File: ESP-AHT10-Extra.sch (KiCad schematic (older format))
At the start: 29 parts, among them J1 USB, SW1 RESET, SW2 PROG, U1 CH330N, U2 HT7233, U3 ESP-12, U4 AHT10, U5 USBLC6-2SC6

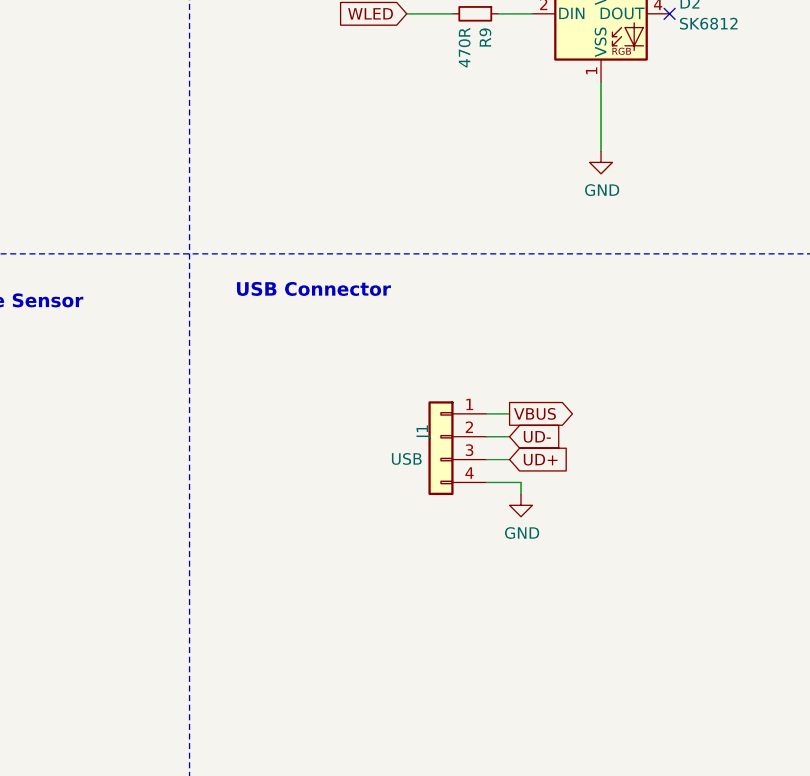
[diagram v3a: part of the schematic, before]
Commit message: place WLED, tidy up after some footprint changes
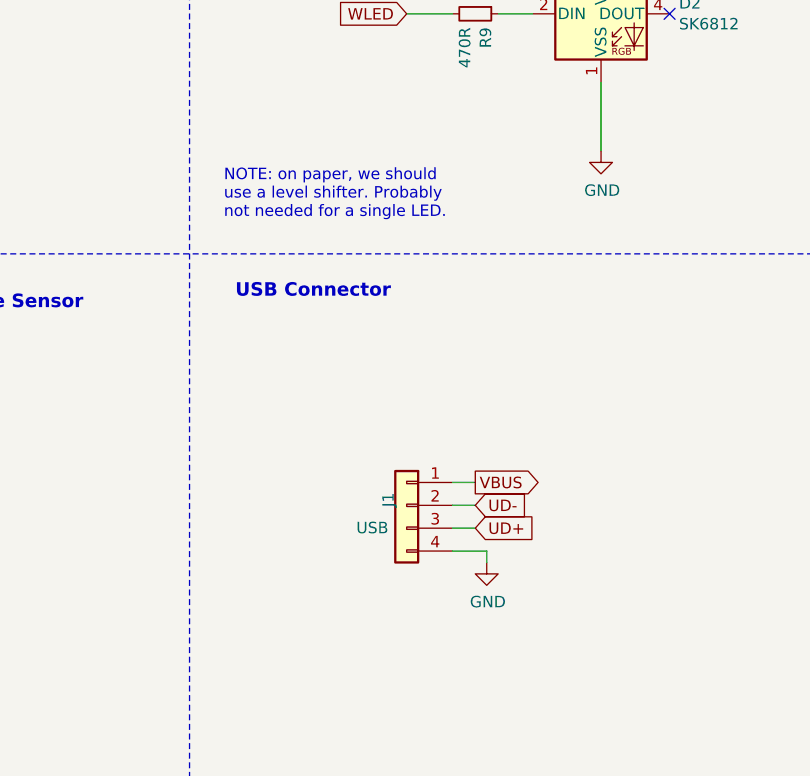
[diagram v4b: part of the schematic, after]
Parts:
- C1, C2, C3, C4, C5, C6, C7, C8: footprint Capacitors_SMD:C_0805 -> Capacitor_SMD:C_0805_2012Metric
- C9: footprint (none) -> Capacitor_SMD:C_0805_2012Metric
- D1: footprint Diodes_SMD:D_SOD-123F -> Diode_SMD:D_SOD-123F
- R1, R2, R3, R4, R5, R6, R7, R8, R9: footprint Resistors_SMD:R_0805 -> Resistor_SMD:R_0805_2012Metric
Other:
- note added: "NOTE: on paper, we should\nuse a level shifter. Probably\nnot needed for a single LED."
- moved on the sheet: J1
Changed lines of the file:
@@
 L Connector_Generic:Conn_01x04 J1
 U 1 1 5DBDB3F6
-P 5550 3100
-F 0 "J1" V 5630 3092 50  0000 L CNN
-F 1 "USB" H 5630 3001 50  0000 L CNN
-F 2 "CPB:usb-PCB" H 5550 3100 50  0001 C CNN
-F 3 "~" H 5550 3100 50  0001 C CNN
-	1    5550 3100
+P 5400 3400
+F 0 "J1" V 5480 3392 50  0000 L CNN
+F 1 "USB" H 5480 3301 50  0000 L CNN
+F 2 "CPB:usb-PCB" H 5400 3400 50  0001 C CNN
+F 3 "~" H 5400 3400 50  0001 C CNN
+	1    5400 3400
 	-1   0    0    -1
 $EndComp
@@
 F 0 "R4" H 3709 6946 50  0000 L CNN
 F 1 "10K" H 3709 6855 50  0000 L CNN
-F 2 "Resistors_SMD:R_0805" H 3650 6900 50  0001 C CNN
+F 2 "Resistor_SMD:R_0805_2012Metric" H 3650 6900 50  0001 C CNN
 F 3 "~" H 3650 6900 50  0001 C CNN
 	1    3650 6900
@@
 F 0 "R1" H 1159 5846 50  0000 L CNN
 F 1 "10K" H 1159 5755 50  0000 L CNN
-F 2 "Resistors_SMD:R_0805" H 1100 5800 50  0001 C CNN
+F 2 "Resistor_SMD:R_0805_2012Metric" H 1100 5800 50  0001 C CNN
 F 3 "~" H 1100 5800 50  0001 C CNN
 	1    1100 5800
@@
 F 0 "C1" H 1042 6296 50  0000 L CNN
 F 1 "100n" H 1042 6205 50  0000 L CNN
-F 2 "Capacitors_SMD:C_0805" H 950 6250 50  0001 C CNN
+F 2 "Capacitor_SMD:C_0805_2012Metric" H 950 6250 50  0001 C CNN
 F 3 "~" H 950 6250 50  0001 C CNN
 	1    950  6250
@@
 F 0 "R5" H 3759 5696 50  0000 L CNN
 F 1 "10K" H 3759 5605 50  0000 L CNN
-F 2 "Resistors_SMD:R_0805" H 3700 5650 50  0001 C CNN
+F 2 "Resistor_SMD:R_0805_2012Metric" H 3700 5650 50  0001 C CNN
 F 3 "~" H 3700 5650 50  0001 C CNN
 	1    3700 5650
@@
 F 0 "R2" V 1354 5900 50  0000 C CNN
 F 1 "1K" V 1445 5900 50  0000 C CNN
-F 2 "Resistors_SMD:R_0805" H 1550 5900 50  0001 C CNN
+F 2 "Resistor_SMD:R_0805_2012Metric" H 1550 5900 50  0001 C CNN
 F 3 "~" H 1550 5900 50  0001 C CNN
 	1    1550 5900
@@
 F 0 "C2" H 1892 1646 50  0000 L CNN
 F 1 "10u" H 1892 1555 50  0000 L CNN
-F 2 "Capacitors_SMD:C_0805" H 1800 1600 50  0001 C CNN
+F 2 "Capacitor_SMD:C_0805_2012Metric" H 1800 1600 50  0001 C CNN
 F 3 "~" H 1800 1600 50  0001 C CNN
 	1    1800 1600
@@
 F 0 "C4" H 3292 1646 50  0000 L CNN
 F 1 "10u" H 3292 1555 50  0000 L CNN
-F 2 "Capacitors_SMD:C_0805" H 3200 1600 50  0001 C CNN
+F 2 "Capacitor_SMD:C_0805_2012Metric" H 3200 1600 50  0001 C CNN
 F 3 "~" H 3200 1600 50  0001 C CNN
 	1    3200 1600
@@
 F 0 "R7" H 3359 3196 50  0000 L CNN
 F 1 "10K" H 3359 3105 50  0000 L CNN
-F 2 "Resistors_SMD:R_0805" H 3300 3150 50  0001 C CNN
+F 2 "Resistor_SMD:R_0805_2012Metric" H 3300 3150 50  0001 C CNN
 F 3 "~" H 3300 3150 50  0001 C CNN
 	1    3300 3150
@@
 F 0 "R6" H 3059 3196 50  0000 L CNN
 F 1 "10K" H 3059 3105 50  0000 L CNN
-F 2 "Resistors_SMD:R_0805" H 3000 3150 50  0001 C CNN
+F 2 "Resistor_SMD:R_0805_2012Metric" H 3000 3150 50  0001 C CNN
 F 3 "~" H 3000 3150 50  0001 C CNN
 	1    3000 3150
@@
 F 0 "C5" H 1742 3146 50  0000 L CNN
 F 1 "100n" H 1742 3055 50  0000 L CNN
-F 2 "Capacitors_SMD:C_0805" H 1650 3100 50  0001 C CNN
+F 2 "Capacitor_SMD:C_0805_2012Metric" H 1650 3100 50  0001 C CNN
 F 3 "~" H 1650 3100 50  0001 C CNN
 	1    1650 3100
@@
 F 0 "R3" H 1759 5546 50  0000 L CNN
 F 1 "10K" H 1759 5455 50  0000 L CNN
-F 2 "Resistors_SMD:R_0805" H 1700 5500 50  0001 C CNN
+F 2 "Resistor_SMD:R_0805_2012Metric" H 1700 5500 50  0001 C CNN
 F 3 "~" H 1700 5500 50  0001 C CNN
 	1    1700 5500
@@
 	1    0    0    -1
 $EndComp
-Text GLabel 5850 3100 2    50   Input ~ 0
+Text GLabel 5700 3400 2    50   Input ~ 0
 UD-
-Text GLabel 5850 3200 2    50   Input ~ 0
+Text GLabel 5700 3500 2    50   Input ~ 0
 UD+
 Text GLabel 10600 3600 2    50   Input ~ 0
@@
 F 0 "C3" V 7721 5150 50  0000 C CNN
 F 1 "100n" V 7812 5150 50  0000 C CNN
-F 2 "Capacitors_SMD:C_0805" H 7950 5150 50  0001 C CNN
+F 2 "Capacitor_SMD:C_0805_2012Metric" H 7950 5150 50  0001 C CNN
 F 3 "~" H 7950 5150 50  0001 C CNN
 	1    7950 5150
@@
 F 0 "C6" V 8221 5450 50  0000 C CNN
 F 1 "100n" V 8312 5450 50  0000 C CNN
-F 2 "Capacitors_SMD:C_0805" H 8450 5450 50  0001 C CNN
+F 2 "Capacitor_SMD:C_0805_2012Metric" H 8450 5450 50  0001 C CNN
 F 3 "~" H 8450 5450 50  0001 C CNN
 	1    8450 5450
@@
 L power:GND #PWR0101
 U 1 1 5DC645A4
-P 5900 3350
-F 0 "#PWR0101" H 5900 3100 50  0001 C CNN
-F 1 "GND" H 5905 3177 50  0000 C CNN
-F 2 "" H 5900 3350 50  0001 C CNN
-F 3 "" H 5900 3350 50  0001 C CNN
-	1    5900 3350
-	1    0    0    -1
-$EndComp
-Text GLabel 5850 3000 2    50   Output ~ 0
+P 5750 3650
+F 0 "#PWR0101" H 5750 3400 50  0001 C CNN
+F 1 "GND" H 5755 3477 50  0000 C CNN
+F 2 "" H 5750 3650 50  0001 C CNN
+F 3 "" H 5750 3650 50  0001 C CNN
+	1    5750 3650
+	1    0    0    -1
+$EndComp
+Text GLabel 5700 3300 2    50   Output ~ 0
 VBUS
 Text GLabel 1050 1350 0    50   Input ~ 0
 VBUS
 Wire Wire Line
-	5750 3000 5850 3000
-Wire Wire Line
-	5750 3100 5850 3100
-Wire Wire Line
-	5750 3200 5850 3200
-Wire Wire Line
-	5750 3300 5900 3300
-Wire Wire Line
-	5900 3300 5900 3350
+	5600 3300 5700 3300
+Wire Wire Line
+	5600 3400 5700 3400
+Wire Wire Line
+	5600 3500 5700 3500
+Wire Wire Line
+	5600 3600 5750 3600
+Wire Wire Line
+	5750 3600 5750 3650
 Text GLabel 3350 1000 2    50   Output ~ 0
 5V
@@
 F 0 "C7" V 10221 2850 50  0000 C CNN
 F 1 "100n" V 10312 2850 50  0000 C CNN
-F 2 "Capacitors_SMD:C_0805" H 10450 2850 50  0001 C CNN
+F 2 "Capacitor_SMD:C_0805_2012Metric" H 10450 2850 50  0001 C CNN
 F 3 "~" H 10450 2850 50  0001 C CNN
 	1    10450 2850
@@
 F 0 "R8" H 9759 5596 50  0000 L CNN
 F 1 "470R" H 9759 5505 50  0000 L CNN
-F 2 "Resistors_SMD:R_0805" H 9700 5550 50  0001 C CNN
+F 2 "Resistor_SMD:R_0805_2012Metric" H 9700 5550 50  0001 C CNN
 F 3 "~" H 9700 5550 50  0001 C CNN
 	1    9700 5550
@@
 F 0 "D1" H 1250 1145 50  0000 C CNN
 F 1 "B5817W" H 1250 1236 50  0000 C CNN
-F 2 "Diodes_SMD:D_SOD-123F" V 1250 1350 50  0001 C CNN
+F 2 "Diode_SMD:D_SOD-123F" V 1250 1350 50  0001 C CNN
 F 3 "~" V 1250 1350 50  0001 C CNN
 	1    1250 1350
@@
 F 0 "C8" H 7692 5196 50  0000 L CNN
 F 1 "10u" H 7692 5105 50  0000 L CNN
-F 2 "Capacitors_SMD:C_0805" H 7600 5150 50  0001 C CNN
+F 2 "Capacitor_SMD:C_0805_2012Metric" H 7600 5150 50  0001 C CNN
 F 3 "~" H 7600 5150 50  0001 C CNN
 	1    7600 5150
@@
 F 0 "R9" H 5759 1296 50  0000 L CNN
 F 1 "470R" H 5759 1205 50  0000 L CNN
-F 2 "Resistors_SMD:R_0805" H 5700 1250 50  0001 C CNN
+F 2 "Resistor_SMD:R_0805_2012Metric" H 5700 1250 50  0001 C CNN
 F 3 "~" H 5700 1250 50  0001 C CNN
 	1    5700 1250
@@
 F 0 "C9" V 6371 850 50  0000 C CNN
 F 1 "47u" V 6462 850 50  0000 C CNN
-F 2 "" H 6600 850 50  0001 C CNN
+F 2 "Capacitor_SMD:C_0805_2012Metric" H 6600 850 50  0001 C CNN
 F 3 "~" H 6600 850 50  0001 C CNN
 	1    6600 850
@@
 Text Notes 4650 700  0    59   ~ 12
 Nightlight
+Text Notes 4600 2150 0    50   ~ 0
+NOTE: on paper, we should\nuse a level shifter. Probably\nnot needed for a single LED.
 $EndSCHEMATC

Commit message: more tweaking
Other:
- note added: "This might need a\n100nF decoupling cap."
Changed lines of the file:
@@
 Text Notes 4600 2150 0    50   ~ 0
 NOTE: on paper, we should\nuse a level shifter. Probably\nnot needed for a single LED.
+Text Notes 6800 700  0    50   ~ 0
+This might need a\n100nF decoupling cap.
 $EndSCHEMATC

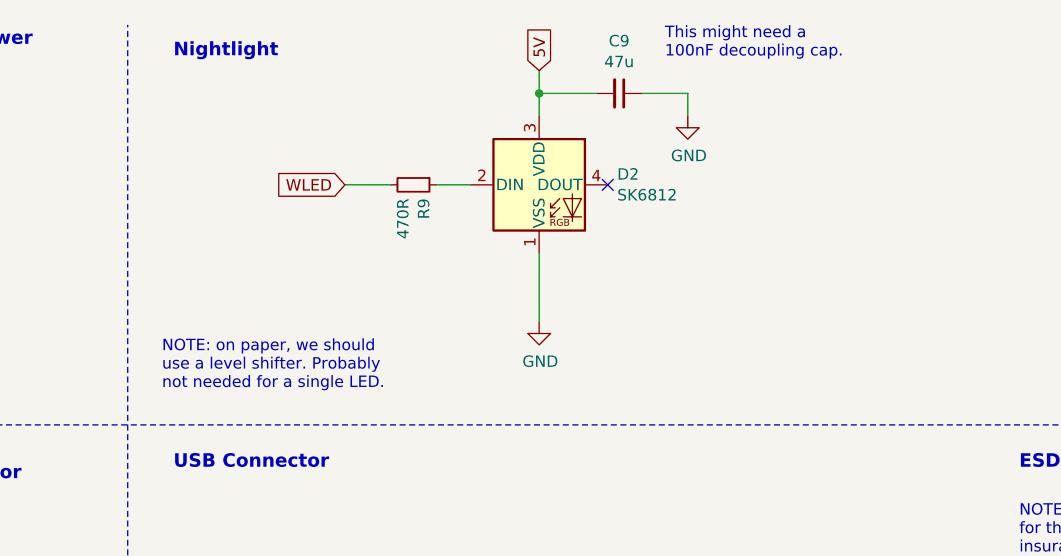
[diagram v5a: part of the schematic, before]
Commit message: drop the nightlight concept; it's not going to work with the power dissipation of a WLED. Clean things up for double-sided milling a bit more.
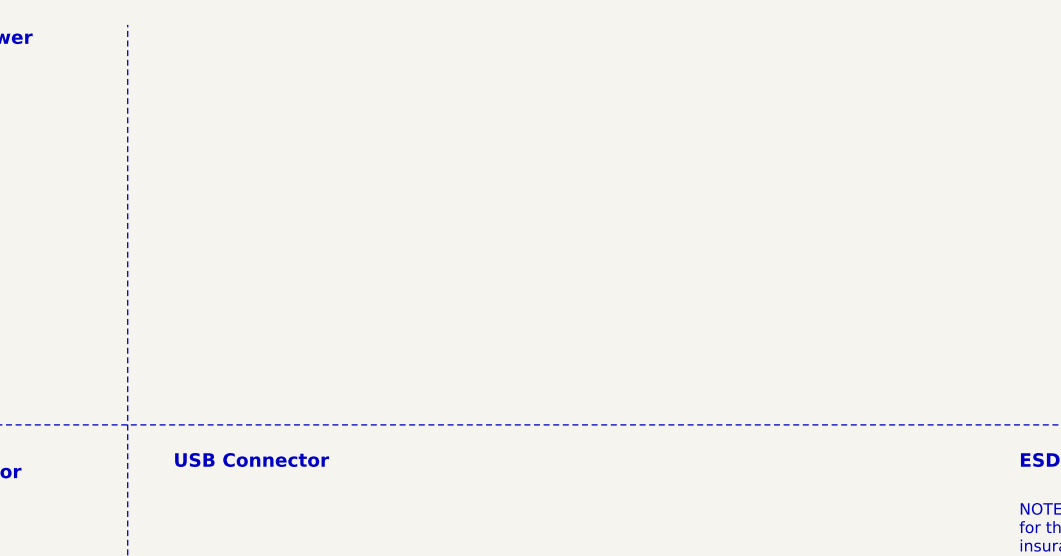
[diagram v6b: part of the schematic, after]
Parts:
- removed C9: 47u, Capacitor_SMD:C_0805_2012Metric, symbol Device:C_Small
- removed D2: SK6812, LED_SMD:LED_SK6812_PLCC4_5.0x5.0mm_P3.2mm, symbol LED:SK6812
- removed R9: 470R, Resistor_SMD:R_0805_2012Metric, symbol Device:R_Small
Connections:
- no-connect marks 5 -> 4
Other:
- note removed: "NOTE: on paper, we should\nuse a level shifter. Probably\nnot needed for a single LED."
- note removed: "Nightlight"
- note removed: "This might need a\n100nF decoupling cap."
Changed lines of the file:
@@
 Wire Notes Line
 	4450 7700 4450 550
-$Comp
-L LED:SK6812 D2
-U 1 1 5DD551FE
-P 6250 1250
-F 0 "D2" H 6591 1296 50  0000 L CNN
-F 1 "SK6812" H 6591 1205 50  0000 L CNN
-F 2 "LED_SMD:LED_SK6812_PLCC4_5.0x5.0mm_P3.2mm" H 6300 950 50  0001 L TNN
-F 3 "https://cdn-shop.adafruit.com/product-files/1138/SK6812+LED+datasheet+.pdf" H 6350 875 50  0001 L TNN
-	1    6250 1250
-	1    0    0    -1
-$EndComp
 Text GLabel 1750 6300 0    50   Output ~ 0
 WLED
-Text GLabel 5400 1250 0    50   Input ~ 0
-WLED
-$Comp
-L Device:R_Small R9
-U 1 1 5DD55710
-P 5700 1250
-F 0 "R9" H 5759 1296 50  0000 L CNN
-F 1 "470R" H 5759 1205 50  0000 L CNN
-F 2 "Resistor_SMD:R_0805_2012Metric" H 5700 1250 50  0001 C CNN
-F 3 "~" H 5700 1250 50  0001 C CNN
-	1    5700 1250
-	0    1    1    0
-$EndComp
-Text GLabel 6250 750  1    50   Input ~ 0
-5V
-$Comp
-L power:GND #PWR07
-U 1 1 5DD58857
-P 6250 1850
-F 0 "#PWR07" H 6250 1600 50  0001 C CNN
-F 1 "GND" H 6255 1677 50  0000 C CNN
-F 2 "" H 6250 1850 50  0001 C CNN
-F 3 "" H 6250 1850 50  0001 C CNN
-	1    6250 1850
-	1    0    0    -1
-$EndComp
-NoConn ~ 6550 1250
-$Comp
-L Device:C_Small C9
-U 1 1 5DD5E86C
-P 6600 850
-F 0 "C9" V 6371 850 50  0000 C CNN
-F 1 "47u" V 6462 850 50  0000 C CNN
-F 2 "Capacitor_SMD:C_0805_2012Metric" H 6600 850 50  0001 C CNN
-F 3 "~" H 6600 850 50  0001 C CNN
-	1    6600 850
-	0    1    1    0
-$EndComp
-Wire Wire Line
-	5400 1250 5600 1250
-Wire Wire Line
-	5800 1250 5950 1250
-Wire Wire Line
-	6250 750  6250 850
-Wire Wire Line
-	6250 1550 6250 1850
-$Comp
-L power:GND #PWR08
-U 1 1 5DD6B19B
-P 6900 950
-F 0 "#PWR08" H 6900 700 50  0001 C CNN
-F 1 "GND" H 6905 777 50  0000 C CNN
-F 2 "" H 6900 950 50  0001 C CNN
-F 3 "" H 6900 950 50  0001 C CNN
-	1    6900 950
-	1    0    0    -1
-$EndComp
-Wire Wire Line
-	6250 850  6500 850
-Connection ~ 6250 850
-Wire Wire Line
-	6250 850  6250 950
-Wire Wire Line
-	6700 850  6900 850
-Wire Wire Line
-	6900 850  6900 950
-Text Notes 4650 700  0    59   ~ 12
-Nightlight
-Text Notes 4600 2150 0    50   ~ 0
-NOTE: on paper, we should\nuse a level shifter. Probably\nnot needed for a single LED.
-Text Notes 6800 700  0    50   ~ 0
-This might need a\n100nF decoupling cap.
 $EndSCHEMATC

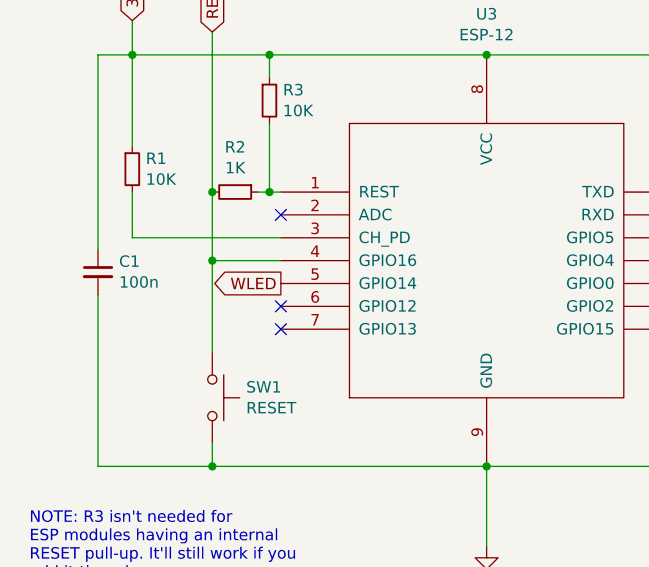
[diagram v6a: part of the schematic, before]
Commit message: minor silk tweaks
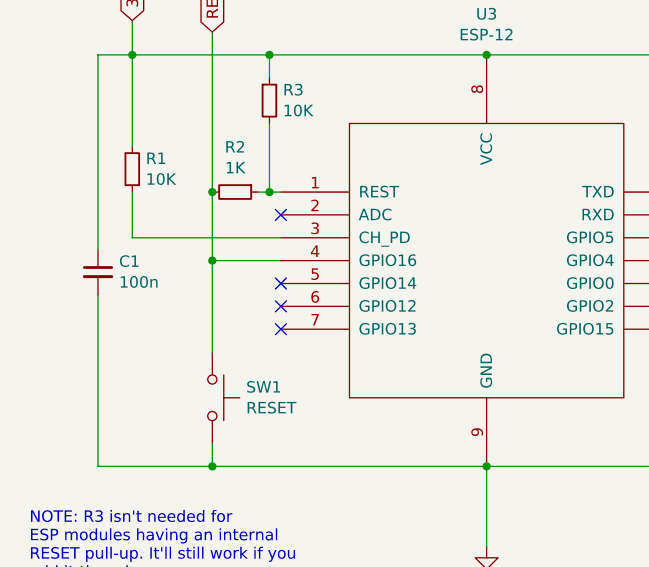
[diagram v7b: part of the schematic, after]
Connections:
- net WLED: no longer names the net of U3.5 (GPIO14)
- no-connect marks 4 -> 5
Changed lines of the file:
@@
 Title ""
 Date ""
-Rev ""
+Rev "1.4"
 Comp ""
 Comment1 ""
@@
 Wire Notes Line
 	4450 7700 4450 550
-Text GLabel 1750 6300 0    50   Output ~ 0
-WLED
+NoConn ~ 1750 6300
 $EndSCHEMATC

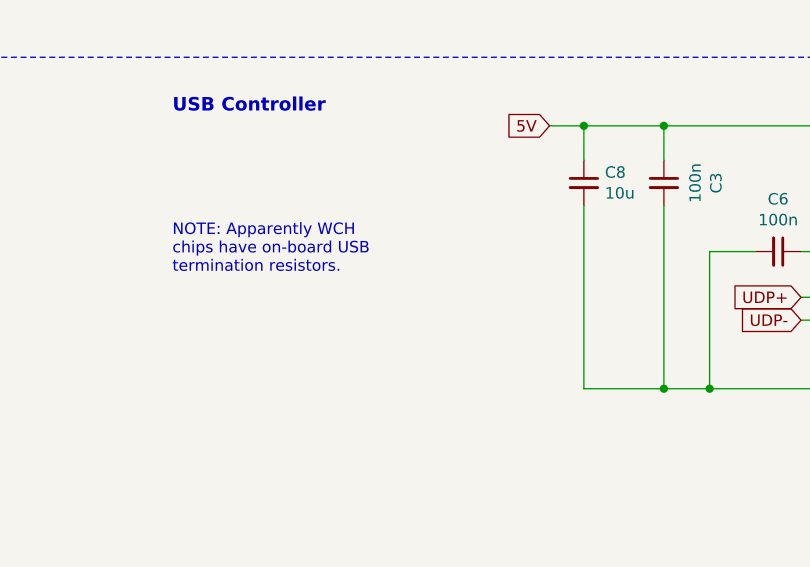
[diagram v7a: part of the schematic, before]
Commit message: some notes on the CH330N running on 5V.
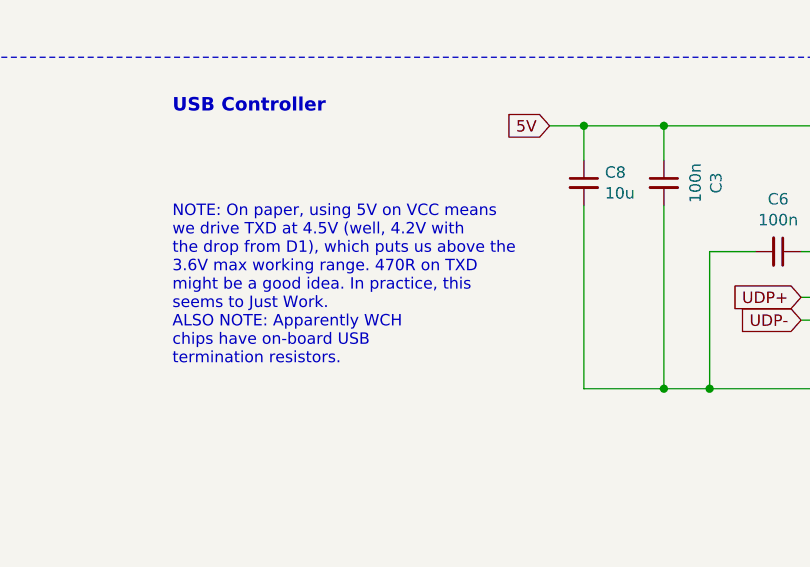
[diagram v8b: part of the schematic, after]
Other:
- note added: "NOTE: On paper, using 5V on VCC means\nwe drive TXD at 4.5V (well, 4.2V with\nthe drop from D1), which puts us above the\n3.6V max working range. 470R on TXD\nmight be a good idea. In practice, this\nseems to Just Work.\nALSO NOTE: Apparently WCH\nchips have on-board USB\ntermination resistors."
- note removed: "NOTE: Apparently WCH\nchips have on-board USB\ntermination resistors."
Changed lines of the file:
@@
 Wire Wire Line
 	10600 2850 10600 3000
-Text Notes 5800 5550 0    50   ~ 0
-NOTE: Apparently WCH\nchips have on-board USB\ntermination resistors.
+Text Notes 5800 5950 0    50   ~ 0
+NOTE: On paper, using 5V on VCC means\nwe drive TXD at 4.5V (well, 4.2V with\nthe drop from D1), which puts us above the\n3.6V max working range. 470R on TXD\nmight be a good idea. In practice, this\nseems to Just Work.\nALSO NOTE: Apparently WCH\nchips have on-board USB\ntermination resistors.
 Wire Wire Line
 	8150 6050 9150 6050
